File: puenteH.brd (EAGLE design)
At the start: 100 x 80 mm, 20 parts, among them IC1 LM393N, Q1 IRF4905, Q2 IRLZ44Z, Q3 IRLZ44Z, Q4 IRF4905, Q5 IRF540, Q6 IRF540, Q7 IRF9530, Q8 IRF9530

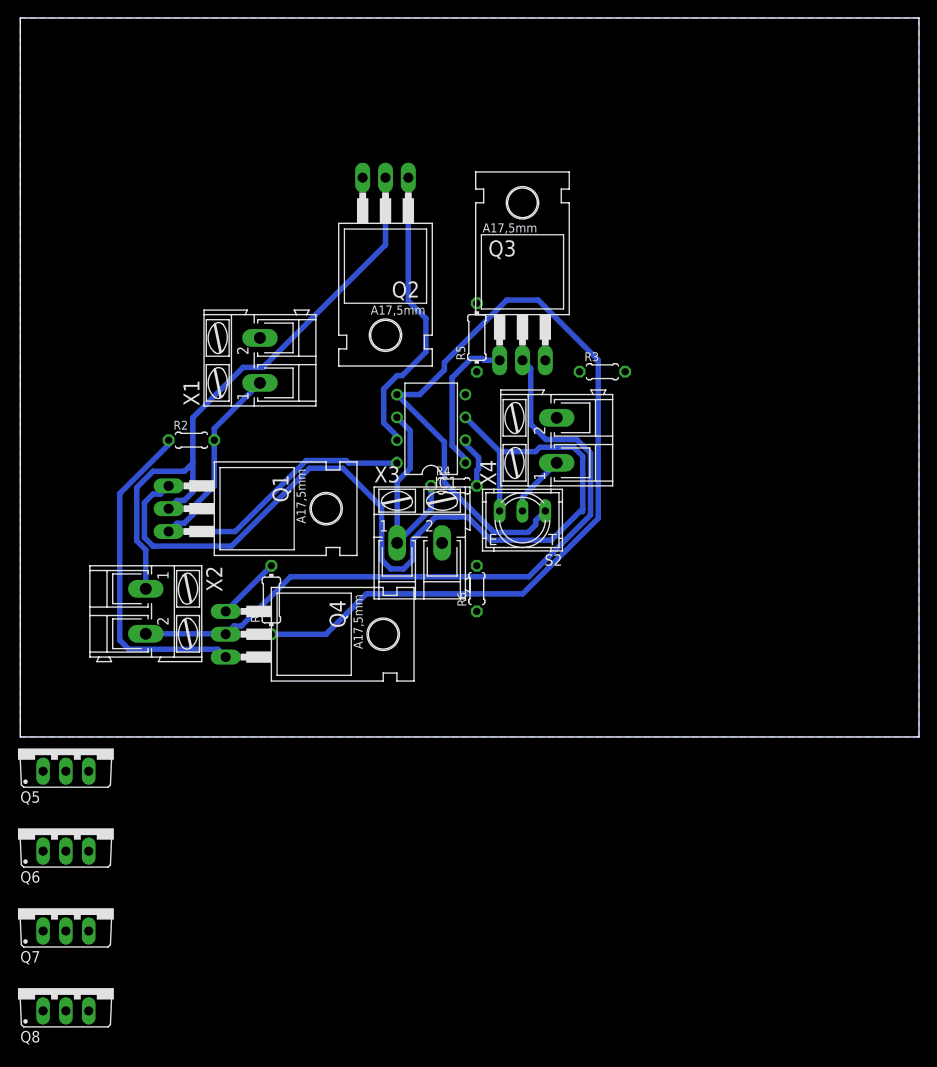
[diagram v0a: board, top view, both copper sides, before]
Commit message: Ready to get gerbers, a little optimized, not using 'compontents that are really going to be used' but it is good enough
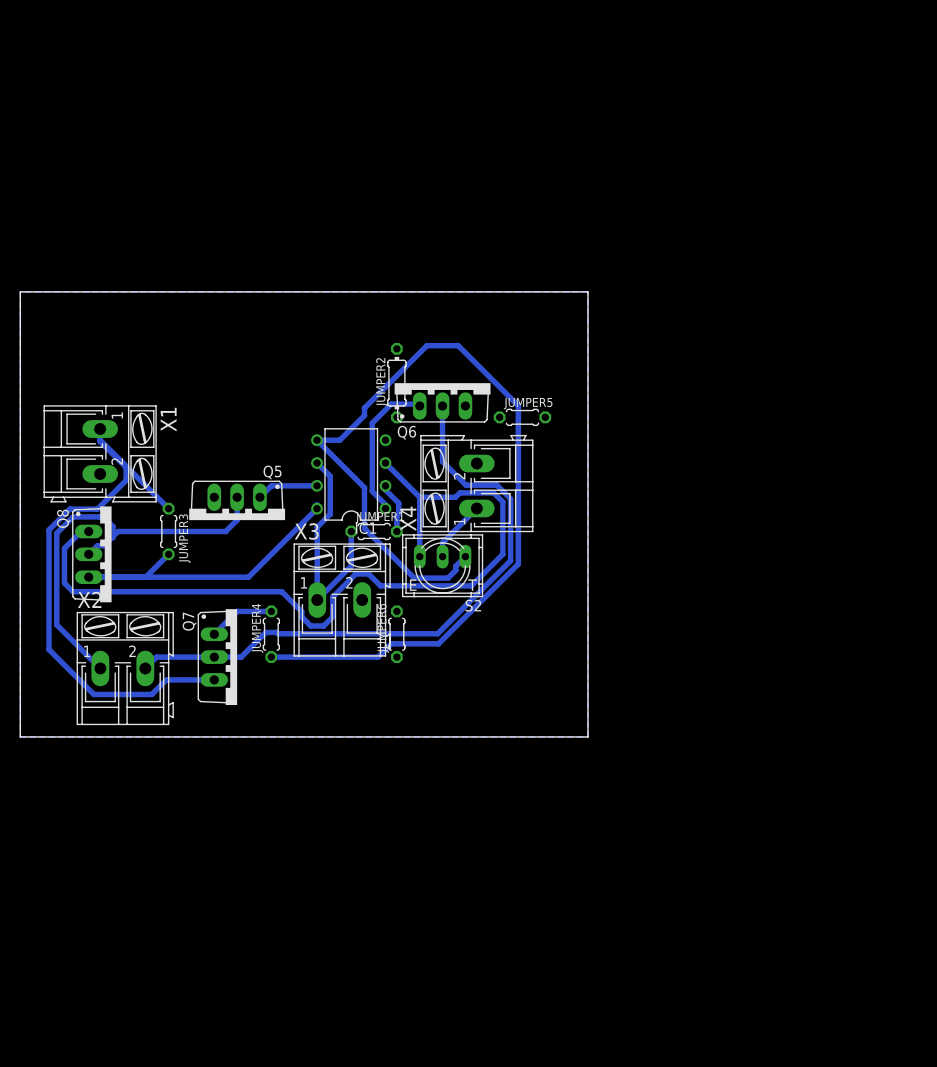
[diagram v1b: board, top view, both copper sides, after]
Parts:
- removed Q1, Q4: IRF4905, transistor-power:TO220BH
- removed Q2, Q3: IRLZ44Z, transistor-power:TO220BH
- removed R1, R5: (no value), rcl:0204/7
- removed R2, R3, R4, R6: (no value), rcl:0204/5
- added JUMPER1, JUMPER3, JUMPER4, JUMPER5, JUMPER6: (no value), rcl:0204/5
- added JUMPER2: (no value), rcl:0204/7
- moved Q6 64.9 mm to (47.0, 39.4)
- moved Q8 48.5 mm to (10.2, 20.3), turned to 270 degrees
- moved Q7 33.8 mm to (24.1, 8.89), turned to 270 degrees
- moved Q5 31.8 mm to (24.1, 24.1), turned to 180 degrees
- moved X1 20.5 mm to (8.89, 31.8), turned to 270 degrees
- moved X3 10.9 mm to (35.6, 15.2)
- moved IC1 10.2 mm to (36.8, 29.2)
- moved S2 10.2 mm to (47.0, 19.1)
- moved X4 10.2 mm to (50.8, 27.9)
- moved X2 6.84 mm to (11.4, 7.62), turned to 0 degrees
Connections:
- net 0: now also JUMPER2.1, JUMPER2.2, JUMPER5.1, JUMPER5.2, JUMPER6.1, JUMPER6.2, Q5.S, Q6.S; no longer Q2.S, Q3.S, R3.1, R3.2, R5.1, R5.2, R6.1, R6.2
- net DER: now also Q8.G; no longer Q1.G
- net IZQ: now also JUMPER4.1, JUMPER4.2, Q7.G; no longer Q4.G, R1.1, R1.2
- net MOTOR_DER: now also Q6.D, Q7.D; no longer Q3.D, Q4.D
- net MOTOR_IZQ: now also Q5.D, Q8.D; no longer Q1.D, Q2.D
- net PWM: now also JUMPER1.1, JUMPER1.2; no longer R4.1, R4.2
- net VCC: now also JUMPER3.1, JUMPER3.2, Q7.S, Q8.S; no longer Q1.S, Q4.S, R2.1, R2.2
- net VDER: now also Q6.G; no longer Q3.G
- net VIZQ: now also Q5.G; no longer Q2.G
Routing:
- net VIZQ: track 32.9 -> 6.88 mm
- net MOTOR_IZQ: track 67.7 -> 46.5 mm
- net VCC: track 87.5 -> 104.0 mm
- net DER: track 102.4 -> 91.8 mm
- net IZQ: track 123.3 -> 113.6 mm
- net MOTOR_DER: track 77.4 -> 68.1 mm
- net PWM: track 28.9 -> 31.4 mm
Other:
- board size 100 x 80 mm -> 63.2 x 49.5 mm

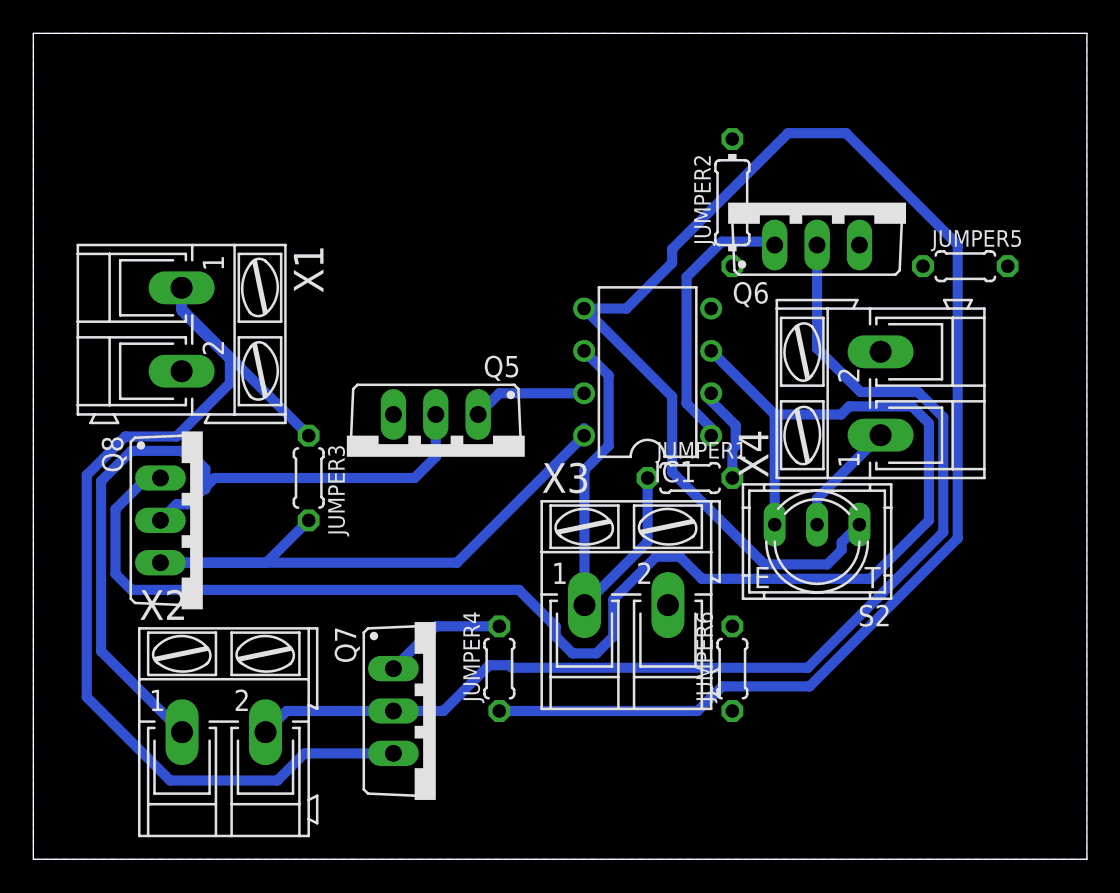
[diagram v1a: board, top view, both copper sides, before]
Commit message: Board compacted a little more. Also added .gitignore
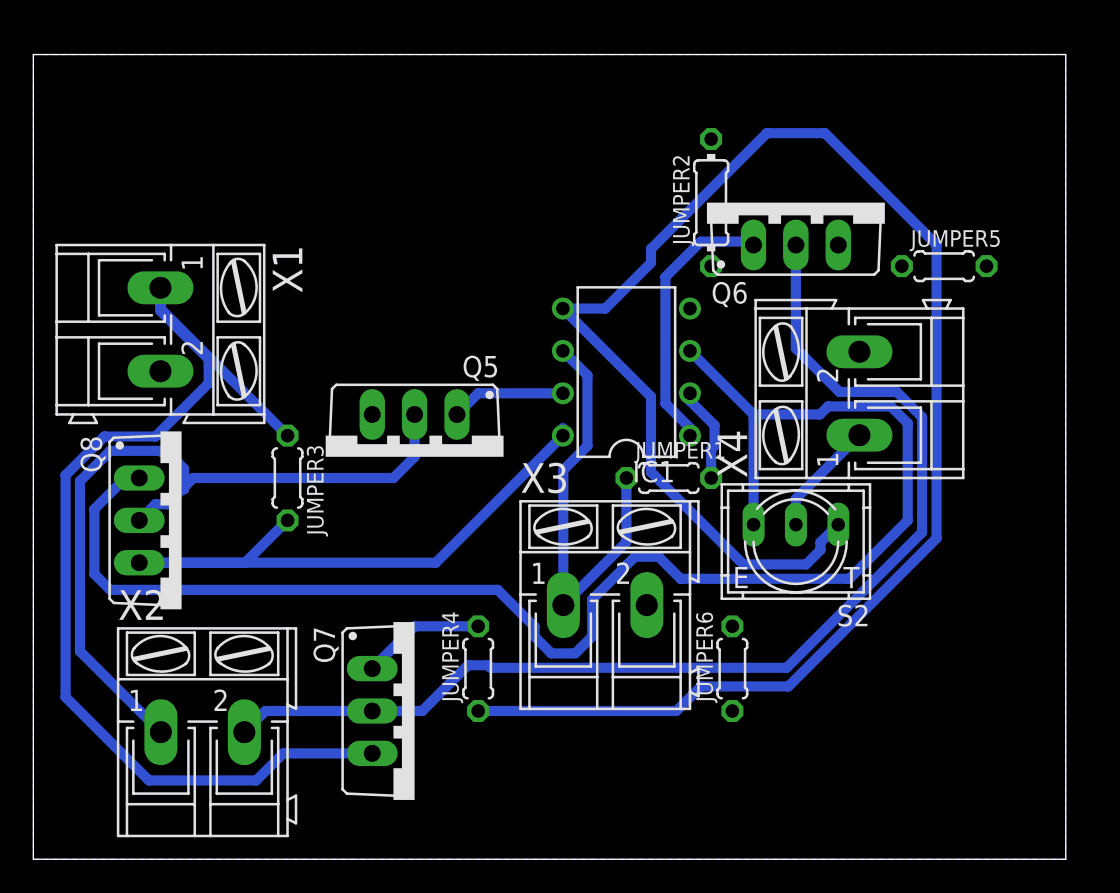
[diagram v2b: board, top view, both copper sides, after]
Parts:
- moved JUMPER5 1.27 mm to (54.6, 35.6)
- moved Q6 1.27 mm to (45.7, 39.4)
- moved S2 1.27 mm to (45.7, 19.1)
- moved X3 1.27 mm to (34.3, 15.2)
- moved JUMPER3 1.27 mm to (15.2, 22.9)
- moved X1 1.27 mm to (7.62, 31.8)
- moved JUMPER4 1.27 mm to (26.7, 11.4)
- moved Q5 1.27 mm to (22.9, 24.1)
- moved Q7 1.27 mm to (22.9, 8.89)
- moved Q8 1.27 mm to (8.89, 20.3)
- moved X2 1.27 mm to (10.2, 7.62)
- moved IC1 1.27 mm to (35.6, 29.2)
- moved JUMPER1 1.27 mm to (38.1, 22.9)
- moved JUMPER2 1.27 mm to (40.6, 39.4)
- moved X4 1.27 mm to (49.5, 27.9)
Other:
- board size 63.2 x 49.5 mm -> 61.9 x 48.2 mm
